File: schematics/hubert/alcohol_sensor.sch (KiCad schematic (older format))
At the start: 1 part

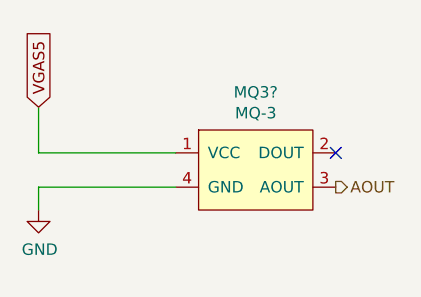
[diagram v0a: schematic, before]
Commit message: updated schematics
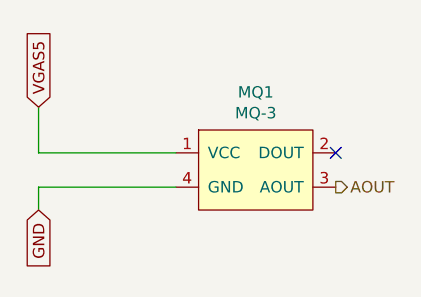
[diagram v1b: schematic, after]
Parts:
- gave numbers to parts that had none: 1
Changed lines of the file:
@@
 $Descr A4 11693 8268
 encoding utf-8
-Sheet 6 6
-Title ""
-Date ""
-Rev ""
+Sheet 6 7
+Title "Hubert"
+Date "2018-11-02"
+Rev "1.1"
 Comp ""
 Comment1 ""
@@
 $EndDescr
 $Comp
-L mq3:MQ-3 MQ3?
+L mq3:MQ-3 MQ1
 U 1 1 5BDB6A31
 P 4650 3050
-F 0 "MQ3?" H 4650 3365 50  0000 C CNN
+F 0 "MQ1" H 4650 3365 50  0000 C CNN
 F 1 "MQ-3" H 4650 3274 50  0000 C CNN
 F 2 "" H 4400 3300 50  0001 C CNN
 F 3 "" H 4400 3300 50  0001 C CNN
 	1    4650 3050
-	1    0    0    -1
-$EndComp
-$Comp
-L power:GND #PWR?
-U 1 1 5BDB6AC5
-P 3700 3250
-F 0 "#PWR?" H 3700 3000 50  0001 C CNN
-F 1 "GND" H 3705 3077 50  0000 C CNN
-F 2 "" H 3700 3250 50  0001 C CNN
-F 3 "" H 3700 3250 50  0001 C CNN
-	1    3700 3250
 	1    0    0    -1
 $EndComp
@@
 Text GLabel 3700 2800 1    50   Input ~ 0
 VGAS5
+Text GLabel 3700 3250 3    50   Input ~ 0
+GND
 $EndSCHEMATC

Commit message: fixed ERC problems and added connector for input pins
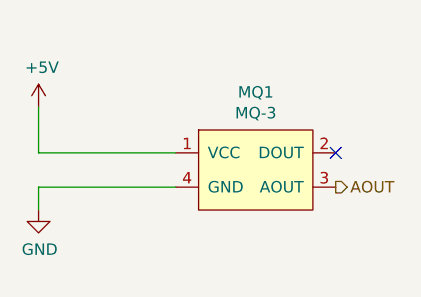
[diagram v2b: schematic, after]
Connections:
- net VGAS5 renamed +5V
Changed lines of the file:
@@
 Text HLabel 5000 3150 2    50   Output ~ 0
 AOUT
-Text GLabel 3700 2800 1    50   Input ~ 0
-VGAS5
-Text GLabel 3700 3250 3    50   Input ~ 0
-GND
+$Comp
+L power:GND #PWR0125
+U 1 1 5BE2CD67
+P 3700 3250
+F 0 "#PWR0125" H 3700 3000 50  0001 C CNN
+F 1 "GND" H 3705 3077 50  0000 C CNN
+F 2 "" H 3700 3250 50  0001 C CNN
+F 3 "" H 3700 3250 50  0001 C CNN
+	1    3700 3250
+	1    0    0    -1
+$EndComp
+$Comp
+L power:+5V #PWR0126
+U 1 1 5BE2CDA7
+P 3700 2800
+F 0 "#PWR0126" H 3700 2650 50  0001 C CNN
+F 1 "+5V" H 3715 2973 50  0000 C CNN
+F 2 "" H 3700 2800 50  0001 C CNN
+F 3 "" H 3700 2800 50  0001 C CNN
+	1    3700 2800
+	1    0    0    -1
+$EndComp
 $EndSCHEMATC
